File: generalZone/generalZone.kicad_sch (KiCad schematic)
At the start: 20 parts, among them M1 Motor_Servo, M10 Motor_Servo, M11 Motor_Servo, M12 Motor_Servo, M13 Motor_Servo, M14 Motor_Servo, M15 Motor_Servo, M16 Motor_Servo, M17 Motor_Servo, M18 Motor_Servo, M2 Motor_Servo, M3 Motor_Servo, M4 Motor_Servo, M5 Motor_Servo, M6 Motor_Servo, M7 Motor_Servo, M8 Motor_Servo, M9 Motor_Servo, U1 PCA9685

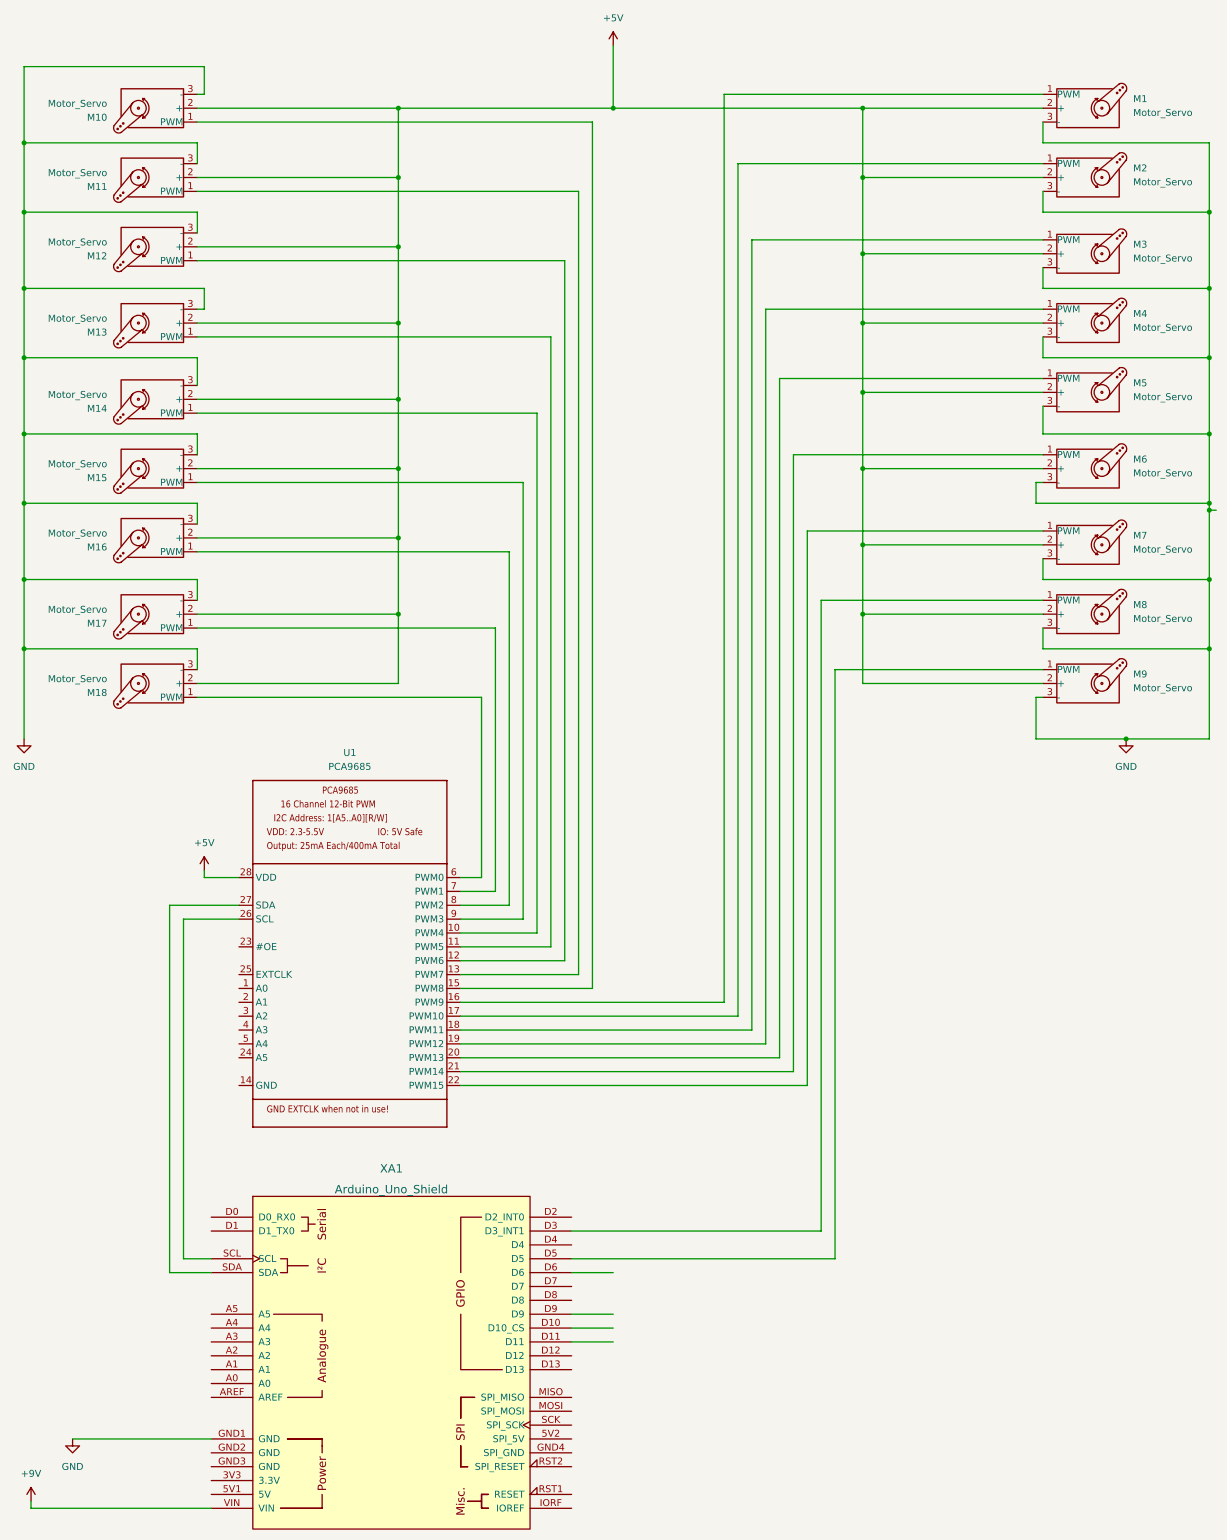
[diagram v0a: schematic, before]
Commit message: colored the wires
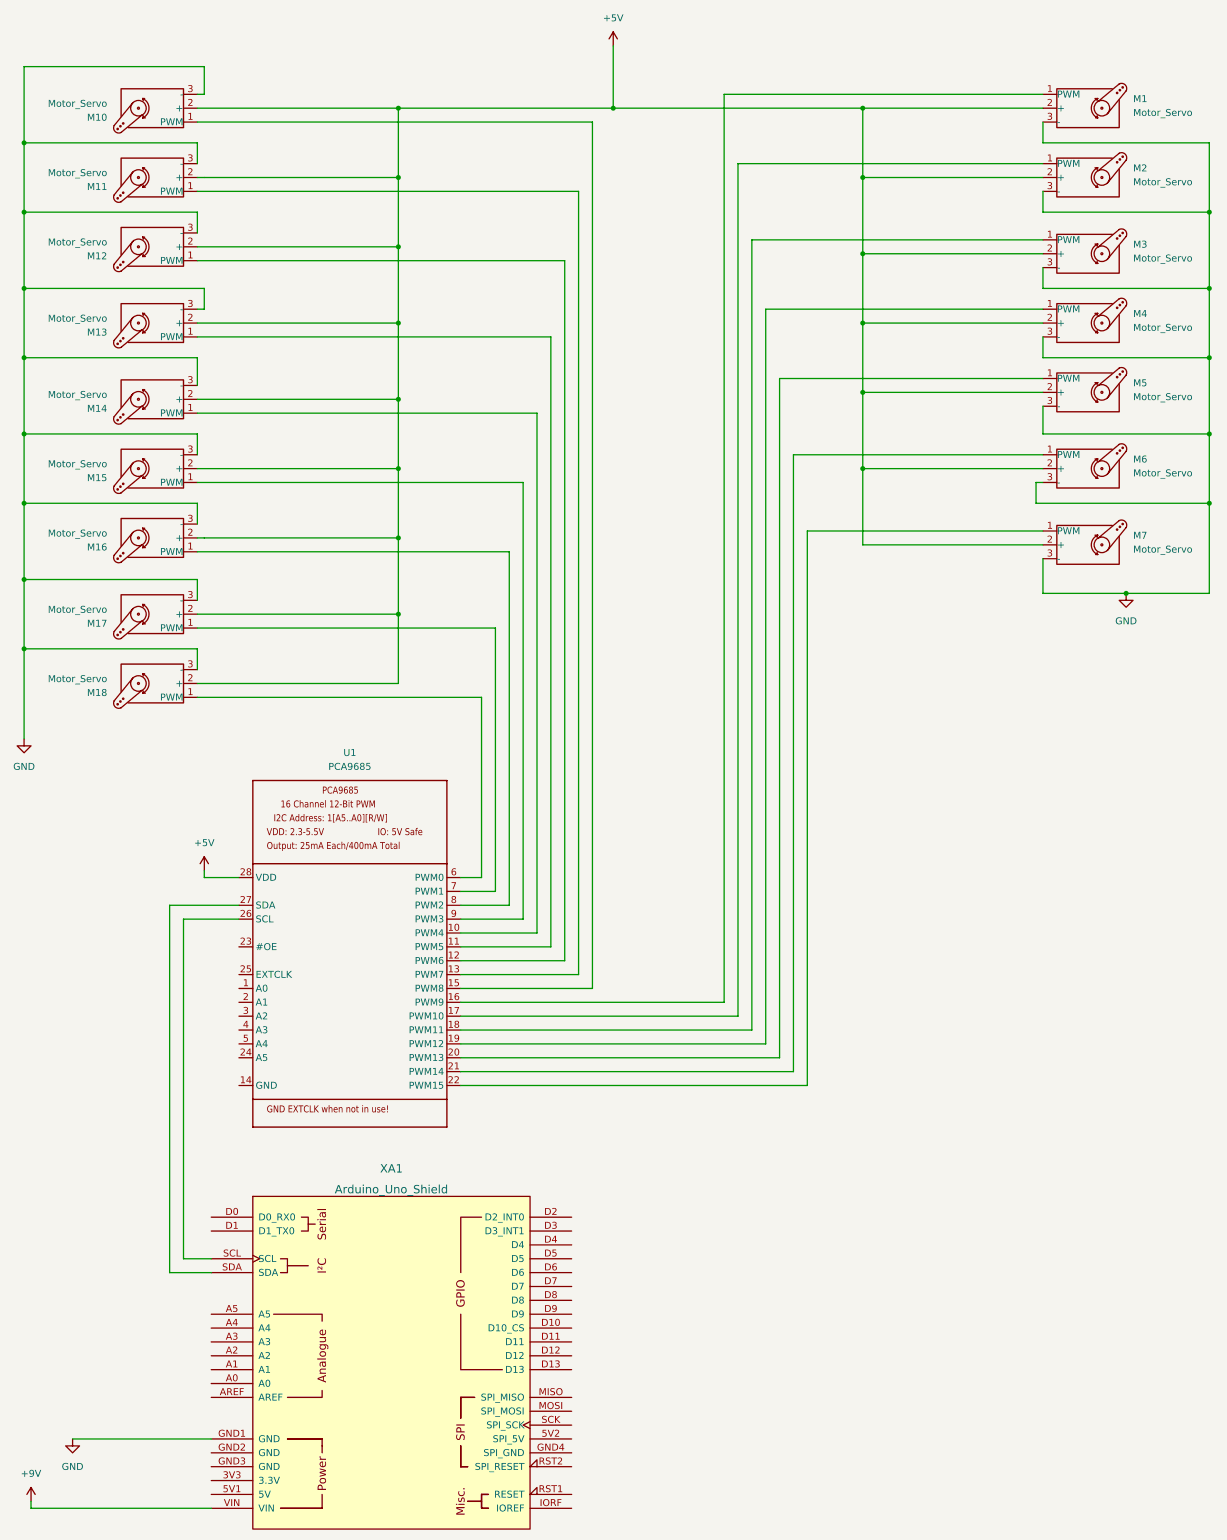
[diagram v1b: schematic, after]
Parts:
- removed M8, M9: Motor_Servo, symbol Motor:Motor_Servo
